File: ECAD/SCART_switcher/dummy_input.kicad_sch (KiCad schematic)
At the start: 40 parts

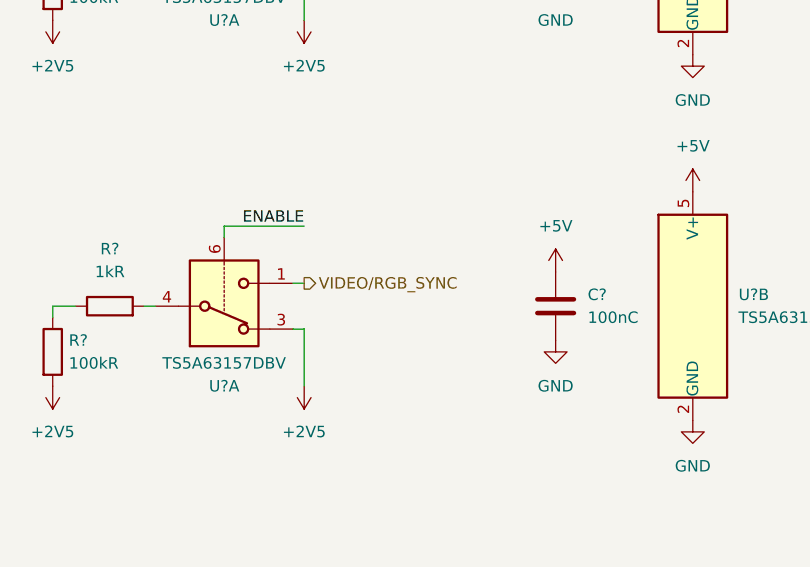
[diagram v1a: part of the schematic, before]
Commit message: ERC fixes.
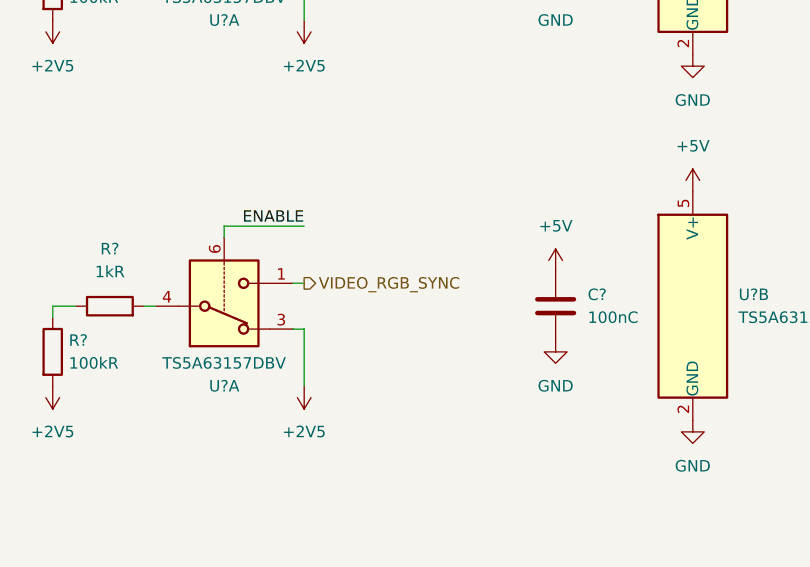
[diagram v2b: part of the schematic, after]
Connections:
- net VIDEO/RGB_SYNC renamed VIDEO_RGB_SYNC
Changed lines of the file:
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@@
     (effects (font (size 1.27 1.27)) (justify left))
   )
-  (hierarchical_label "VIDEO{slash}RGB_SYNC" (shape output) (at 191.77 120.65 0) (fields_autoplaced)
+  (hierarchical_label "VIDEO_RGB_SYNC" (shape output) (at 191.77 120.65 0) (fields_autoplaced)
     (effects (font (size 1.27 1.27)) (justify left))
   )
@@
         )
         (path "/8cd08eb5-4755-4ef5-8eeb-77fd9974b180/45065d08-b417-4621-b4a4-65949829b8d7"
-          (reference "#PWR0401") (unit 1)
+          (reference "#PWR0402") (unit 1)
         )
       )
@@
         )
         (path "/8cd08eb5-4755-4ef5-8eeb-77fd9974b180/45065d08-b417-4621-b4a4-65949829b8d7"
-          (reference "#PWR0399") (unit 1)
+          (reference "#PWR0400") (unit 1)
         )
       )
@@
         )
         (path "/8cd08eb5-4755-4ef5-8eeb-77fd9974b180/45065d08-b417-4621-b4a4-65949829b8d7"
-          (reference "#PWR0429") (unit 1)
+          (reference "#PWR0430") (unit 1)
         )
       )
@@
         )
         (path "/8cd08eb5-4755-4ef5-8eeb-77fd9974b180/45065d08-b417-4621-b4a4-65949829b8d7"
-          (reference "#PWR0396") (unit 1)
+          (reference "#PWR0397") (unit 1)
         )
       )
@@
         )
         (path "/8cd08eb5-4755-4ef5-8eeb-77fd9974b180/45065d08-b417-4621-b4a4-65949829b8d7"
-          (reference "#PWR0415") (unit 1)
+          (reference "#PWR0416") (unit 1)
         )
       )
@@
         )
         (path "/8cd08eb5-4755-4ef5-8eeb-77fd9974b180/45065d08-b417-4621-b4a4-65949829b8d7"
-          (reference "#PWR0425") (unit 1)
+          (reference "#PWR0426") (unit 1)
         )
       )
@@
         )
         (path "/8cd08eb5-4755-4ef5-8eeb-77fd9974b180/45065d08-b417-4621-b4a4-65949829b8d7"
-          (reference "#PWR0421") (unit 1)
+          (reference "#PWR0422") (unit 1)
         )
       )
@@
         )
         (path "/8cd08eb5-4755-4ef5-8eeb-77fd9974b180/45065d08-b417-4621-b4a4-65949829b8d7"
-          (reference "#PWR0434") (unit 1)
+          (reference "#PWR0435") (unit 1)
         )
       )
@@
         )
         (path "/8cd08eb5-4755-4ef5-8eeb-77fd9974b180/45065d08-b417-4621-b4a4-65949829b8d7"
-          (reference "#PWR0422") (unit 1)
+          (reference "#PWR0423") (unit 1)
         )
       )
@@
         )
         (path "/8cd08eb5-4755-4ef5-8eeb-77fd9974b180/45065d08-b417-4621-b4a4-65949829b8d7"
-          (reference "#PWR0417") (unit 1)
+          (reference "#PWR0418") (unit 1)
         )
       )
@@
         )
         (path "/8cd08eb5-4755-4ef5-8eeb-77fd9974b180/45065d08-b417-4621-b4a4-65949829b8d7"
-          (reference "#PWR0410") (unit 1)
+          (reference "#PWR0411") (unit 1)
         )
       )
@@
         )
         (path "/8cd08eb5-4755-4ef5-8eeb-77fd9974b180/45065d08-b417-4621-b4a4-65949829b8d7"
-          (reference "#PWR0395") (unit 1)
+          (reference "#PWR0396") (unit 1)
         )
       )
@@
         )
         (path "/8cd08eb5-4755-4ef5-8eeb-77fd9974b180/45065d08-b417-4621-b4a4-65949829b8d7"
-          (reference "#PWR0405") (unit 1)
+          (reference "#PWR0406") (unit 1)
         )
       )
@@
         )
         (path "/8cd08eb5-4755-4ef5-8eeb-77fd9974b180/45065d08-b417-4621-b4a4-65949829b8d7"
-          (reference "#PWR0414") (unit 1)
+          (reference "#PWR0415") (unit 1)
         )
       )
@@
         )
         (path "/8cd08eb5-4755-4ef5-8eeb-77fd9974b180/45065d08-b417-4621-b4a4-65949829b8d7"
-          (reference "#PWR0419") (unit 1)
+          (reference "#PWR0420") (unit 1)
         )
       )
@@
         )
         (path "/8cd08eb5-4755-4ef5-8eeb-77fd9974b180/45065d08-b417-4621-b4a4-65949829b8d7"
-          (reference "#PWR0431") (unit 1)
+          (reference "#PWR0432") (unit 1)
         )
       )
@@
         )
         (path "/8cd08eb5-4755-4ef5-8eeb-77fd9974b180/45065d08-b417-4621-b4a4-65949829b8d7"
-          (reference "#PWR0418") (unit 1)
+          (reference "#PWR0419") (unit 1)
         )
       )
@@
         )
         (path "/8cd08eb5-4755-4ef5-8eeb-77fd9974b180/45065d08-b417-4621-b4a4-65949829b8d7"
-          (reference "#PWR0404") (unit 1)
+          (reference "#PWR0405") (unit 1)
         )
       )
@@
         )
         (path "/8cd08eb5-4755-4ef5-8eeb-77fd9974b180/45065d08-b417-4621-b4a4-65949829b8d7"
-          (reference "#PWR0403") (unit 1)
+          (reference "#PWR0404") (unit 1)
         )
       )
@@
         )
         (path "/8cd08eb5-4755-4ef5-8eeb-77fd9974b180/45065d08-b417-4621-b4a4-65949829b8d7"
-          (reference "#PWR0427") (unit 1)
+          (reference "#PWR0428") (unit 1)
         )
       )
@@
         )
         (path "/8cd08eb5-4755-4ef5-8eeb-77fd9974b180/45065d08-b417-4621-b4a4-65949829b8d7"
-          (reference "#PWR0411") (unit 1)
+          (reference "#PWR0412") (unit 1)
         )
       )
@@
         )
         (path "/8cd08eb5-4755-4ef5-8eeb-77fd9974b180/45065d08-b417-4621-b4a4-65949829b8d7"
-          (reference "#PWR0416") (unit 1)
+          (reference "#PWR0417") (unit 1)
         )
       )
@@
         )
         (path "/8cd08eb5-4755-4ef5-8eeb-77fd9974b180/45065d08-b417-4621-b4a4-65949829b8d7"
-          (reference "#PWR0409") (unit 1)
+          (reference "#PWR0410") (unit 1)
         )
       )
@@
         )
         (path "/8cd08eb5-4755-4ef5-8eeb-77fd9974b180/45065d08-b417-4621-b4a4-65949829b8d7"
-          (reference "#PWR0398") (unit 1)
+          (reference "#PWR0399") (unit 1)
         )
       )
@@
         )
         (path "/8cd08eb5-4755-4ef5-8eeb-77fd9974b180/45065d08-b417-4621-b4a4-65949829b8d7"
-          (reference "#PWR0433") (unit 1)
+          (reference "#PWR0434") (unit 1)
         )
       )
@@
         )
         (path "/8cd08eb5-4755-4ef5-8eeb-77fd9974b180/45065d08-b417-4621-b4a4-65949829b8d7"
-          (reference "#PWR0413") (unit 1)
+          (reference "#PWR0414") (unit 1)
         )
       )
@@
         )
         (path "/8cd08eb5-4755-4ef5-8eeb-77fd9974b180/45065d08-b417-4621-b4a4-65949829b8d7"
-          (reference "#PWR0408") (unit 1)
+          (reference "#PWR0409") (unit 1)
         )
       )
@@
         )
         (path "/8cd08eb5-4755-4ef5-8eeb-77fd9974b180/45065d08-b417-4621-b4a4-65949829b8d7"
-          (reference "#PWR0406") (unit 1)
+          (reference "#PWR0407") (unit 1)
         )
       )
@@
         )
         (path "/8cd08eb5-4755-4ef5-8eeb-77fd9974b180/45065d08-b417-4621-b4a4-65949829b8d7"
-          (reference "#PWR0402") (unit 1)
+          (reference "#PWR0403") (unit 1)
         )
       )
@@
         )
         (path "/8cd08eb5-4755-4ef5-8eeb-77fd9974b180/45065d08-b417-4621-b4a4-65949829b8d7"
-          (reference "#PWR0426") (unit 1)
+          (reference "#PWR0427") (unit 1)
         )
       )
@@
         )
         (path "/8cd08eb5-4755-4ef5-8eeb-77fd9974b180/45065d08-b417-4621-b4a4-65949829b8d7"
-          (reference "#PWR0435") (unit 1)
+          (reference "#PWR0436") (unit 1)
         )
       )
@@
         )
         (path "/8cd08eb5-4755-4ef5-8eeb-77fd9974b180/45065d08-b417-4621-b4a4-65949829b8d7"
-          (reference "#PWR0423") (unit 1)
+          (reference "#PWR0424") (unit 1)
         )
       )
@@
         )
         (path "/8cd08eb5-4755-4ef5-8eeb-77fd9974b180/45065d08-b417-4621-b4a4-65949829b8d7"
-          (reference "#PWR0407") (unit 1)
+          (reference "#PWR0408") (unit 1)
         )
       )
@@
         )
         (path "/8cd08eb5-4755-4ef5-8eeb-77fd9974b180/45065d08-b417-4621-b4a4-65949829b8d7"
-          (reference "#PWR0397") (unit 1)
+          (reference "#PWR0398") (unit 1)
         )
       )
@@
         )
         (path "/8cd08eb5-4755-4ef5-8eeb-77fd9974b180/45065d08-b417-4621-b4a4-65949829b8d7"
-          (reference "#PWR0420") (unit 1)
+          (reference "#PWR0421") (unit 1)
         )
       )
@@
         )
         (path "/8cd08eb5-4755-4ef5-8eeb-77fd9974b180/45065d08-b417-4621-b4a4-65949829b8d7"
-          (reference "#PWR0432") (unit 1)
+          (reference "#PWR0433") (unit 1)
         )
       )
@@
         )
         (path "/8cd08eb5-4755-4ef5-8eeb-77fd9974b180/45065d08-b417-4621-b4a4-65949829b8d7"
-          (reference "#PWR0428") (unit 1)
+          (reference "#PWR0429") (unit 1)
         )
       )
@@
         )
         (path "/8cd08eb5-4755-4ef5-8eeb-77fd9974b180/45065d08-b417-4621-b4a4-65949829b8d7"
-          (reference "#PWR0412") (unit 1)
+          (reference "#PWR0413") (unit 1)
         )
       )
@@
         )
         (path "/8cd08eb5-4755-4ef5-8eeb-77fd9974b180/45065d08-b417-4621-b4a4-65949829b8d7"
-          (reference "#PWR0430") (unit 1)
+          (reference "#PWR0431") (unit 1)
         )
       )
@@
         )
         (path "/8cd08eb5-4755-4ef5-8eeb-77fd9974b180/45065d08-b417-4621-b4a4-65949829b8d7"
-          (reference "#PWR0437") (unit 1)
+          (reference "#PWR0438") (unit 1)
         )
       )
@@
         )
         (path "/8cd08eb5-4755-4ef5-8eeb-77fd9974b180/45065d08-b417-4621-b4a4-65949829b8d7"
-          (reference "#PWR0424") (unit 1)
+          (reference "#PWR0425") (unit 1)
         )
       )
@@
         )
         (path "/8cd08eb5-4755-4ef5-8eeb-77fd9974b180/45065d08-b417-4621-b4a4-65949829b8d7"
-          (reference "#PWR0400") (unit 1)
+          (reference "#PWR0401") (unit 1)
         )
       )
@@
         )
         (path "/8cd08eb5-4755-4ef5-8eeb-77fd9974b180/45065d08-b417-4621-b4a4-65949829b8d7"
-          (reference "#PWR0436") (unit 1)
+          (reference "#PWR0437") (unit 1)
         )
       )

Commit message: Progressed ECAD. Error fixing and cleanup.
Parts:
- removed R? (x4): 1kR, Resistor_SMD:R_0805_2012Metric_Pad1.20x1.40mm_HandSolder, symbol Device:R
- removed R? (x2): 20kR, Resistor_SMD:R_0805_2012Metric_Pad1.20x1.40mm_HandSolder, symbol Device:R
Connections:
- net at R?.1: now also U?.4 (x3)
- net at R?.1: now also U?.11, U?.8
- net at R?.1: now also U?.1, U?.4
- net at U?.4: now also R?.1
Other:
- moved on the sheet: Q?, R?

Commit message: Progressed ECAD.
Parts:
- Q?: MFN BC847B,215 -> (none); MPN (none) -> BC847B,215
- R? (x2): MPN (none) -> RC0805FR-0710KL
- U?: MFN 74AHC1G126W5-7 -> (none); MPN (none) -> 74AHC1G126W5-7
- U?: MFN 74AHC1G04W5-7 -> (none); MPN (none) -> 74AHC1G04W5-7
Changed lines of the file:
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@@
       (effects (font (size 1.27 1.27)) hide)
     )
-    (property "MFN" "" (at 39.37 129.54 0)
-      (effects (font (size 1.27 1.27)) hide)
-    )
     (pin "1")
     (pin "2")
@@
       (effects (font (size 1.27 1.27)) (justify left) hide)
     )
-    (property "MFN" "BC847B,215" (at 35.56 41.91 0)
+    (property "MPN" "BC847B,215" (at 35.56 41.91 0)
       (effects (font (size 1.27 1.27)) hide)
     )
@@
       (effects (font (size 1.27 1.27)) hide)
     )
-    (property "MFN" "" (at 250.19 36.83 0)
-      (effects (font (size 1.27 1.27)) hide)
-    )
     (property "MPN" "CL21B104KBCNNNC" (at 250.19 36.83 0)
       (effects (font (size 1.27 1.27)) hide)
@@
       (effects (font (size 1.27 1.27)) hide)
     )
-    (property "MFN" "" (at 163.83 128.27 0)
-      (effects (font (size 1.27 1.27)) hide)
-    )
     (pin "1")
     (pin "2")
@@
       (effects (font (size 1.27 1.27)) hide)
     )
-    (property "MFN" "" (at 219.71 82.55 0)
-      (effects (font (size 1.27 1.27)) hide)
-    )
     (property "MPN" "CL21B104KBCNNNC" (at 219.71 82.55 0)
       (effects (font (size 1.27 1.27)) hide)
@@
       (effects (font (size 1.27 1.27)) hide)
     )
-    (property "Datasheet" "~" (at 38.1 33.02 0)
+    (property "Datasheet" "https://datasheet.lcsc.com/lcsc/1810201611_YAGEO-RC0805FR-0710KL_C84376.pdf" (at 38.1 33.02 0)
+      (effects (font (size 1.27 1.27)) hide)
+    )
+    (property "MPN" "RC0805FR-0710KL" (at 38.1 33.02 0)
       (effects (font (size 1.27 1.27)) hide)
     )
@@
       (effects (font (size 1.27 1.27)) hide)
     )
-    (property "MFN" "" (at 173.99 44.45 0)
-      (effects (font (size 1.27 1.27)) hide)
-    )
     (pin "1")
     (pin "2")
@@
       (effects (font (size 1.27 1.27)) hide)
     )
-    (property "MFN" "74AHC1G126W5-7" (at 127 173.99 0)
+    (property "MPN" "74AHC1G126W5-7" (at 127 173.99 0)
       (effects (font (size 1.27 1.27)) hide)
     )
@@
       (effects (font (size 1.27 1.27)) hide)
     )
-    (property "Datasheet" "~" (at 64.77 45.72 0)
+    (property "Datasheet" "https://datasheet.lcsc.com/lcsc/1810201611_YAGEO-RC0805FR-0710KL_C84376.pdf" (at 64.77 45.72 0)
+      (effects (font (size 1.27 1.27)) hide)
+    )
+    (property "MPN" "RC0805FR-0710KL" (at 64.77 45.72 0)
       (effects (font (size 1.27 1.27)) hide)
     )
@@
       (effects (font (size 1.27 1.27)) hide)
     )
-    (property "MFN" "" (at 39.37 87.63 0)
-      (effects (font (size 1.27 1.27)) hide)
-    )
     (pin "1")
     (pin "2")
@@
       (effects (font (size 1.27 1.27)) hide)
     )
-    (property "MFN" "74AHC1G04W5-7" (at 57.15 173.99 0)
+    (property "MPN" "74AHC1G04W5-7" (at 57.15 173.99 0)
       (effects (font (size 1.27 1.27)) hide)
     )
@@
       (effects (font (size 1.27 1.27)) hide)
     )
-    (property "MFN" "" (at 95.25 82.55 0)
-      (effects (font (size 1.27 1.27)) hide)
-    )
     (property "MPN" "CL21B104KBCNNNC" (at 95.25 82.55 0)
       (effects (font (size 1.27 1.27)) hide)
@@
       (effects (font (size 1.27 1.27)) hide)
     )
-    (property "MFN" "" (at 163.83 87.63 0)
-      (effects (font (size 1.27 1.27)) hide)
-    )
     (pin "1")
     (pin "2")
@@
       (effects (font (size 1.27 1.27)) hide)
     )
-    (property "MFN" "" (at 83.82 173.99 0)
-      (effects (font (size 1.27 1.27)) hide)
-    )
     (property "MPN" "CL21B104KBCNNNC" (at 83.82 173.99 0)
       (effects (font (size 1.27 1.27)) hide)
@@
       (effects (font (size 1.27 1.27)) hide)
     )
-    (property "MFN" "" (at 95.25 124.46 0)
-      (effects (font (size 1.27 1.27)) hide)
-    )
     (property "MPN" "CL21B104KBCNNNC" (at 95.25 124.46 0)
       (effects (font (size 1.27 1.27)) hide)
@@
       (effects (font (size 1.27 1.27)) hide)
     )
-    (property "MFN" "" (at 97.79 44.45 0)
-      (effects (font (size 1.27 1.27)) hide)
-    )
     (pin "1")
     (pin "2")
@@
       (effects (font (size 1.27 1.27)) hide)
     )
-    (property "MFN" "" (at 219.71 123.19 0)
-      (effects (font (size 1.27 1.27)) hide)
-    )
     (property "MPN" "CL21B104KBCNNNC" (at 219.71 123.19 0)
       (effects (font (size 1.27 1.27)) hide)
@@
       (effects (font (size 1.27 1.27)) hide)
     )
-    (property "MFN" "" (at 156.21 173.99 0)
-      (effects (font (size 1.27 1.27)) hide)
-    )

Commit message: Progressed ECAD.
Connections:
- net ~{DUMMY_INPUT_ENABLE} renamed ~{SILENT_OUTPUT_ENABLE}

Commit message: Progressed ECAD.
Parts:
- C? (x7): footprint Capacitor_SMD:C_0805_2012Metric_Pad1.18x1.45mm_HandSolder -> Capacitor_SMD:C_0805_2012Metric
- R? (x10): footprint Resistor_SMD:R_0805_2012Metric_Pad1.20x1.40mm_HandSolder -> Resistor_SMD:R_0805_2012Metric
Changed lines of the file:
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@@
       (effects (font (size 1.27 1.27)))
     )
-    (property "Footprint" "Resistor_SMD:R_0805_2012Metric_Pad1.20x1.40mm_HandSolder" (at 26.67 43.688 90)
+    (property "Footprint" "Resistor_SMD:R_0805_2012Metric" (at 26.67 43.688 90)
       (effects (font (size 1.27 1.27)) hide)
     )
@@
       (effects (font (size 1.27 1.27)) (justify left))
     )
-    (property "Footprint" "Resistor_SMD:R_0805_2012Metric_Pad1.20x1.40mm_HandSolder" (at 37.592 129.54 90)
+    (property "Footprint" "Resistor_SMD:R_0805_2012Metric" (at 37.592 129.54 90)
       (effects (font (size 1.27 1.27)) hide)
     )
@@
       (effects (font (size 1.27 1.27)) (justify left))
     )
-    (property "Footprint" "Capacitor_SMD:C_0805_2012Metric_Pad1.18x1.45mm_HandSolder" (at 251.1552 40.64 0)
+    (property "Footprint" "Capacitor_SMD:C_0805_2012Metric" (at 251.1552 40.64 0)
       (effects (font (size 1.27 1.27)) hide)
     )
@@
       (effects (font (size 1.27 1.27)) (justify left))
     )
-    (property "Footprint" "Resistor_SMD:R_0805_2012Metric_Pad1.20x1.40mm_HandSolder" (at 162.052 128.27 90)
+    (property "Footprint" "Resistor_SMD:R_0805_2012Metric" (at 162.052 128.27 90)
       (effects (font (size 1.27 1.27)) hide)
     )
@@
       (effects (font (size 1.27 1.27)) (justify left))
     )
-    (property "Footprint" "Capacitor_SMD:C_0805_2012Metric_Pad1.18x1.45mm_HandSolder" (at 220.6752 86.36 0)
+    (property "Footprint" "Capacitor_SMD:C_0805_2012Metric" (at 220.6752 86.36 0)
       (effects (font (size 1.27 1.27)) hide)
     )
@@
       (effects (font (size 1.27 1.27)) (justify left))
     )
-    (property "Footprint" "Resistor_SMD:R_0805_2012Metric_Pad1.20x1.40mm_HandSolder" (at 36.322 33.02 90)
+    (property "Footprint" "Resistor_SMD:R_0805_2012Metric" (at 36.322 33.02 90)
       (effects (font (size 1.27 1.27)) hide)
     )
@@
       (effects (font (size 1.27 1.27)) (justify left))
     )
-    (property "Footprint" "Resistor_SMD:R_0805_2012Metric_Pad1.20x1.40mm_HandSolder" (at 172.212 44.45 90)
+    (property "Footprint" "Resistor_SMD:R_0805_2012Metric" (at 172.212 44.45 90)
       (effects (font (size 1.27 1.27)) hide)
     )
@@
       (effects (font (size 1.27 1.27)) (justify left))
     )
-    (property "Footprint" "Resistor_SMD:R_0805_2012Metric_Pad1.20x1.40mm_HandSolder" (at 62.992 45.72 90)
+    (property "Footprint" "Resistor_SMD:R_0805_2012Metric" (at 62.992 45.72 90)
       (effects (font (size 1.27 1.27)) hide)
     )
@@
       (effects (font (size 1.27 1.27)) (justify left))
     )
-    (property "Footprint" "Resistor_SMD:R_0805_2012Metric_Pad1.20x1.40mm_HandSolder" (at 37.592 87.63 90)
+    (property "Footprint" "Resistor_SMD:R_0805_2012Metric" (at 37.592 87.63 90)
       (effects (font (size 1.27 1.27)) hide)
     )
@@
       (effects (font (size 1.27 1.27)))
     )
-    (property "Footprint" "Resistor_SMD:R_0805_2012Metric_Pad1.20x1.40mm_HandSolder" (at 53.34 38.608 90)
+    (property "Footprint" "Resistor_SMD:R_0805_2012Metric" (at 53.34 38.608 90)
       (effects (font (size 1.27 1.27)) hide)
     )
@@
       (effects (font (size 1.27 1.27)) (justify left))
     )
-    (property "Footprint" "Capacitor_SMD:C_0805_2012Metric_Pad1.18x1.45mm_HandSolder" (at 96.2152 86.36 0)
+    (property "Footprint" "Capacitor_SMD:C_0805_2012Metric" (at 96.2152 86.36 0)
       (effects (font (size 1.27 1.27)) hide)
     )
@@
       (effects (font (size 1.27 1.27)) (justify left))
     )
-    (property "Footprint" "Resistor_SMD:R_0805_2012Metric_Pad1.20x1.40mm_HandSolder" (at 162.052 87.63 90)
+    (property "Footprint" "Resistor_SMD:R_0805_2012Metric" (at 162.052 87.63 90)
       (effects (font (size 1.27 1.27)) hide)
     )
@@
       (effects (font (size 1.27 1.27)) (justify left))
     )
-    (property "Footprint" "Capacitor_SMD:C_0805_2012Metric_Pad1.18x1.45mm_HandSolder" (at 84.7852 177.8 0)
+    (property "Footprint" "Capacitor_SMD:C_0805_2012Metric" (at 84.7852 177.8 0)
       (effects (font (size 1.27 1.27)) hide)
     )
@@
       (effects (font (size 1.27 1.27)) (justify left))
     )
-    (property "Footprint" "Capacitor_SMD:C_0805_2012Metric_Pad1.18x1.45mm_HandSolder" (at 96.2152 128.27 0)
+    (property "Footprint" "Capacitor_SMD:C_0805_2012Metric" (at 96.2152 128.27 0)
       (effects (font (size 1.27 1.27)) hide)
     )
@@
       (effects (font (size 1.27 1.27)) (justify left))
     )
-    (property "Footprint" "Resistor_SMD:R_0805_2012Metric_Pad1.20x1.40mm_HandSolder" (at 96.012 44.45 90)
+    (property "Footprint" "Resistor_SMD:R_0805_2012Metric" (at 96.012 44.45 90)
       (effects (font (size 1.27 1.27)) hide)
     )
@@
       (effects (font (size 1.27 1.27)) (justify left))
     )
-    (property "Footprint" "Capacitor_SMD:C_0805_2012Metric_Pad1.18x1.45mm_HandSolder" (at 220.6752 127 0)
+    (property "Footprint" "Capacitor_SMD:C_0805_2012Metric" (at 220.6752 127 0)
       (effects (font (size 1.27 1.27)) hide)
     )
@@
       (effects (font (size 1.27 1.27)) (justify left))
     )
-    (property "Footprint" "Capacitor_SMD:C_0805_2012Metric_Pad1.18x1.45mm_HandSolder" (at 157.1752 177.8 0)
+    (property "Footprint" "Capacitor_SMD:C_0805_2012Metric" (at 157.1752 177.8 0)
       (effects (font (size 1.27 1.27)) hide)
     )
